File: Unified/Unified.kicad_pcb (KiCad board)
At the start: 2 copper layers, 65 x 77.8 mm, 23 parts, among them J1 Conn_Coaxial_Power, J2 Screw_Terminal_01x02, J3 Screw_Terminal_01x02, J4 Conn_01x04_Male, J5 Screw_Terminal_01x04, Q1 IRLB8721PBF, Q2 IRLB8721PBF, Q3 IRLB8721PBF, Q4 IRLB8721PBF, SW1 SW_SPST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

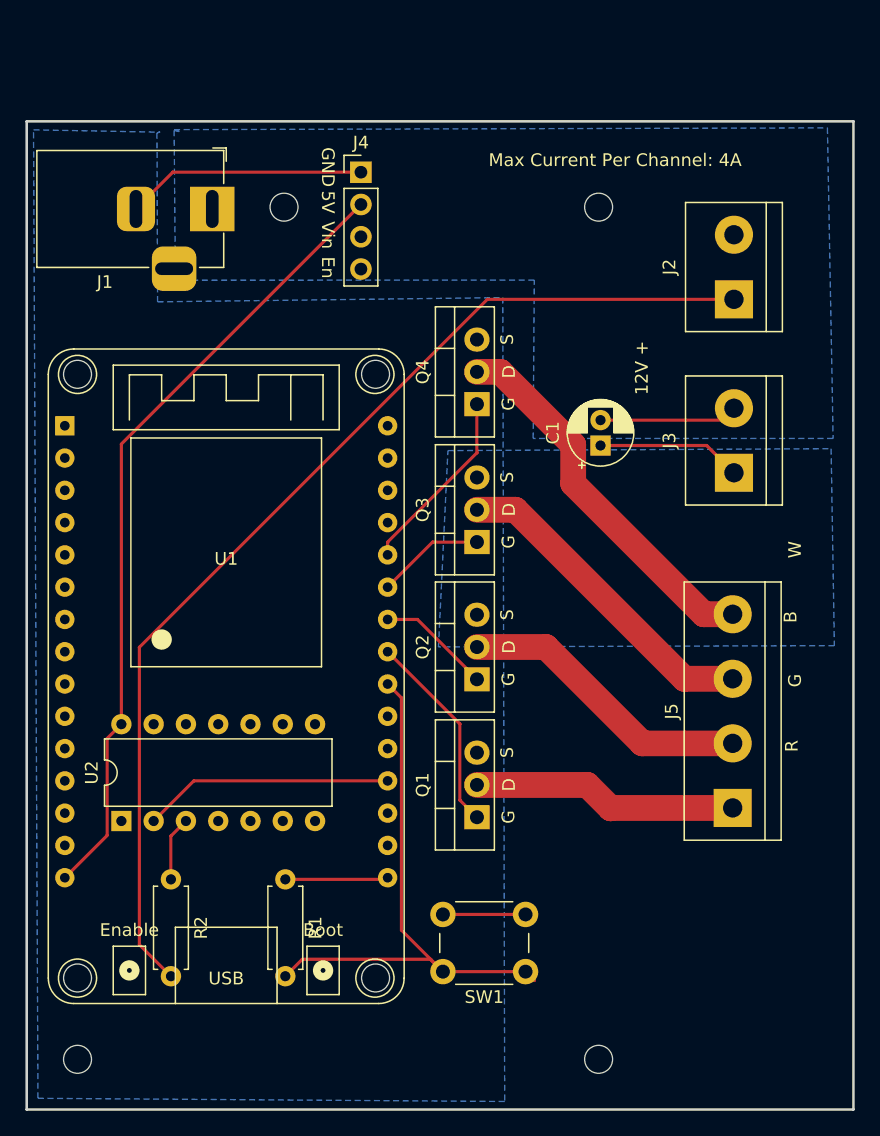
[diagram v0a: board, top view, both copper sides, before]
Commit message: Removes 12V and Ground outputs to LED strip. This will be done with thicker wire outside of PCB, due to high trace width requirements
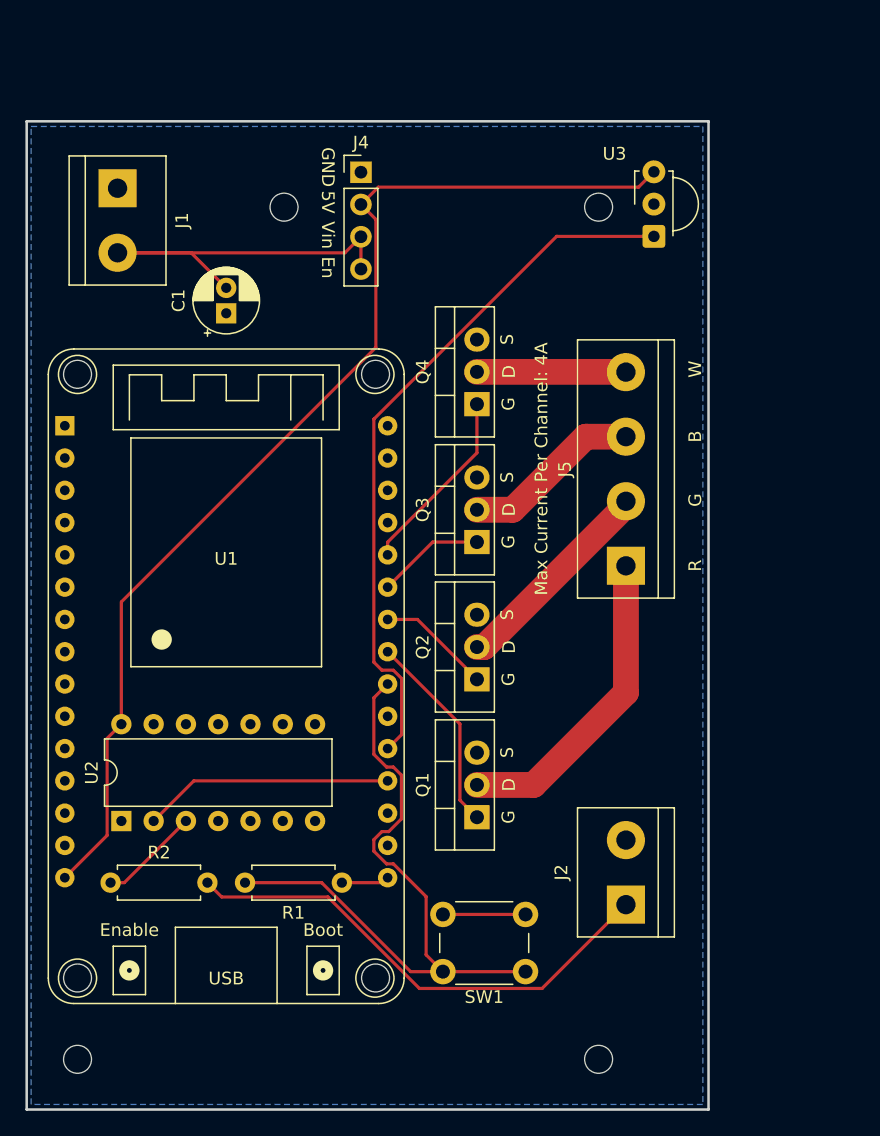
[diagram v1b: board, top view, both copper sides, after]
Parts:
- removed J3: Screw_Terminal_01x02, TerminalBlock:TerminalBlock_bornier-2_P5.08mm
- added U3: TSOP382xx, OptoDevice:Vishay_MINICAST-3Pin, F.Cu at (157.3, 60.9)
- J1: value Conn_Coaxial_Power -> Screw_Terminal_01x02; footprint Connector_BarrelJack:BarrelJack_Horizontal -> TerminalBlock:TerminalBlock_bornier-2_P5.08mm
- moved J2 48.4 mm to (155.1, 113.4)
- moved C1 31.2 mm to (123.7, 66.9)
- moved J5 20.8 mm to (155.1, 86.8)
- moved J1 7.63 mm to (115.1, 57.1), turned to -90 degrees
- moved R2 4.76 mm to (114.5, 111.7), turned to 0 degrees
- moved R1 4.46 mm to (132.8, 111.7), turned to 180 degrees
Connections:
- J1 pad 1: +12V -> GND
- J1 pad 2: GND -> +12V
- U1 pad 20: unconnected-(U1-Pad20) -> Net-(U1-Pad20)
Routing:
- net Net-(U1-Pad20): track 0.00 -> 55.8 mm
- net /D_out: track 85.0 -> 39.1 mm
- net GND: track 36.8 -> 6.50 mm
- net +5V: track 62.6 -> 87.7 mm
- net +12V: track 10.9 -> 31.9 mm
- net LED_W: track 29.8 -> 11.7 mm
- net LED_B: track 25.6 -> 14.1 mm
- net Net-(R1-Pad2): track 45.3 -> 53.0 mm
- net LED_G: track 23.3 -> 16.7 mm
- net +3V3: track 8.10 -> 3.76 mm
- net LED_R: track 20.9 -> 24.7 mm
- net Net-(R2-Pad1): track 5.08 -> 7.94 mm
- removed copper zone on B.Cu, net +12V
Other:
- board size 65 x 77.8 mm -> 53.6 x 77.8 mm
- board text removed: "12V +"

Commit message: Adds custom symbol for the level shifter
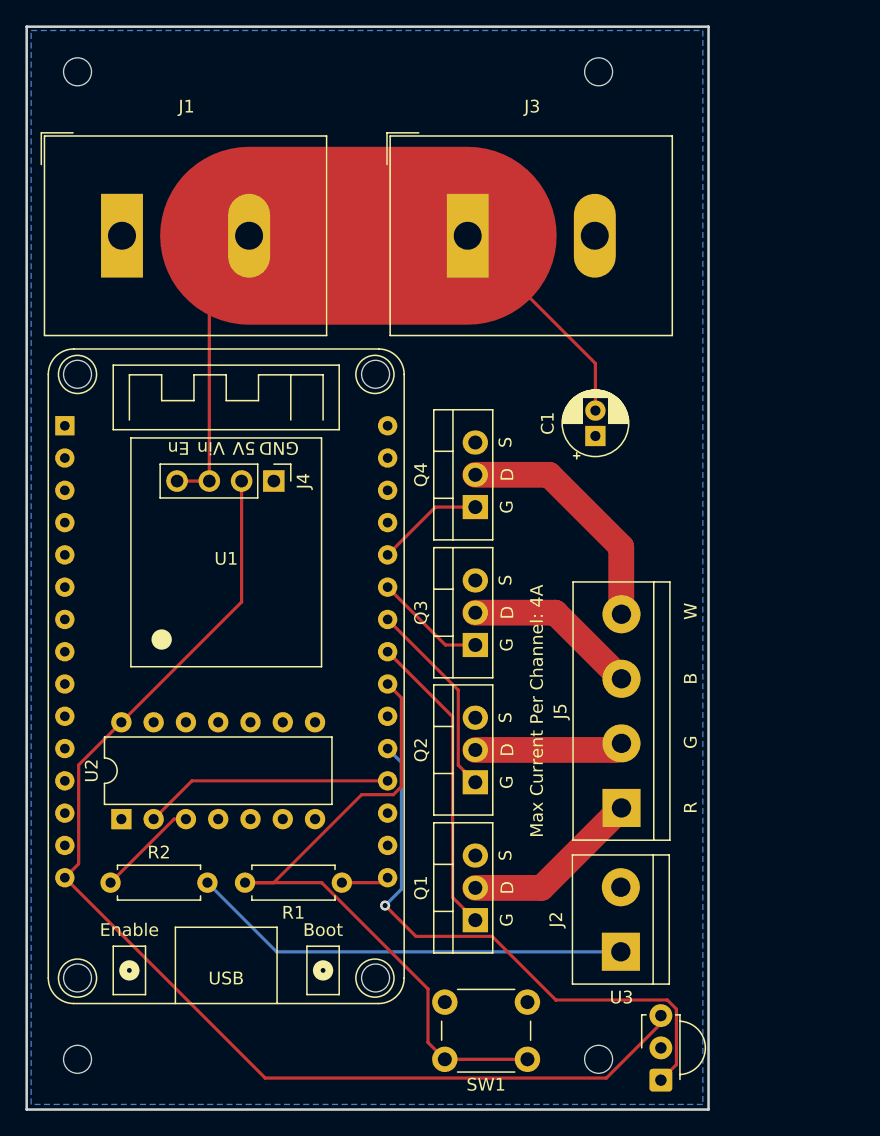
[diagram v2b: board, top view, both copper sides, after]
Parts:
- added J3: Screw_Terminal_01x02, TerminalBlock_Dinkle:TerminalBlock_Dinkle_DT-55-B01X-02_P10.00mm, F.Cu at (142.7, 60.8)
- J1: footprint TerminalBlock:TerminalBlock_bornier-2_P5.08mm -> TerminalBlock_Dinkle:TerminalBlock_Dinkle_DT-55-B01X-02_P10.00mm
- U2: value 74LS125 -> SN74AHCT125
- moved U3 66.4 mm to (157.8, 127.2)
- moved C1 30.6 mm to (152.7, 76.6)
- moved J4 25.2 mm to (127.4, 80.1), turned to -90 degrees
- moved REF** 19.4 mm to (112.0, 47.9)
- moved J5 19.1 mm to (154.8, 105.8)
- moved REF** 10.6 mm to (152.9, 47.9)
- moved Q1 8.10 mm to (143.2, 114.7)
- moved Q4 8.10 mm to (143.2, 82.2)
- moved Q2 8.10 mm to (143.2, 103.8)
- moved Q3 8.10 mm to (143.2, 93.0)
- moved SW1 6.90 mm to (147.3, 125.6)
- moved J1 3.76 mm to (115.5, 60.8), turned to 0 degrees
- moved J2 3.73 mm to (154.7, 117.1)
- moved U2 0.15 mm to (115.4, 106.7)
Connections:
- U2 pad 7: GND -> unconnected-(U2-Pad7)
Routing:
- net +12V: track 31.9 -> 58.3 mm
- net LED_R: track 24.7 -> 14.1 mm
- net Net-(U1-Pad20): track 55.8 -> 45.7 mm, vias 0 -> 1
- net /PWM_R: track 15.9 -> 24.0 mm
- net LED_W: track 11.7 -> 19.1 mm
- net /PWM_G: track 8.99 -> 15.7 mm
- net GND: track 6.50 -> 0.00 mm
- net /PWM_W: track 14.8 -> 8.46 mm
- net +5V: track 87.7 -> 92.8 mm
- net LED_G: track 16.7 -> 12.0 mm
- net /D_out: track 39.1 -> 34.8 mm
- net Net-(R1-Pad2): track 53.0 -> 54.4 mm
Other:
- board size 53.6 x 77.8 mm -> 53.6 x 85.2 mm
